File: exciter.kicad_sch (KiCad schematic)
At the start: 38 parts, among them U5 CC1200, X1 40MHz

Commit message: Add files via upload
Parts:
- removed R2 (x2): 10k, Resistor_SMD:R_0603_1608Metric, symbol Device:R_Small
- renumbered L1 to L2, L2 to L3, L3 to L4, L4 to L5, U5 to U6
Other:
- moved on the sheet: R2

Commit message: partial PN update
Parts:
- C5: PN (none) -> C0603C473K5RACTU
- C5: PN (none) -> C0603C103K5RAC7081
- C5: PN (none) -> C0603C102J5GAC7411
- C5: PN (none) -> C0603C104M5RAC7411
- C5: PN (none) -> GRM1885C1H152JA01D

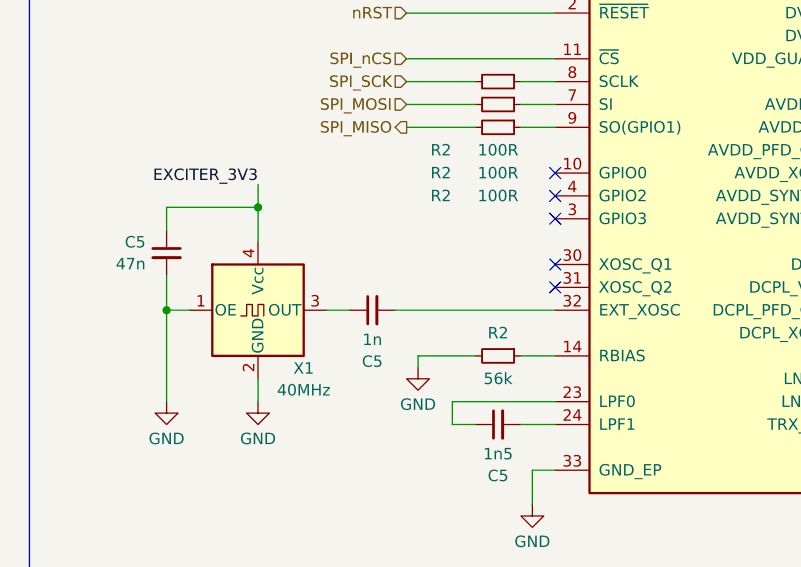
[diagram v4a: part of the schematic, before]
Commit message: added missing 40MHz source
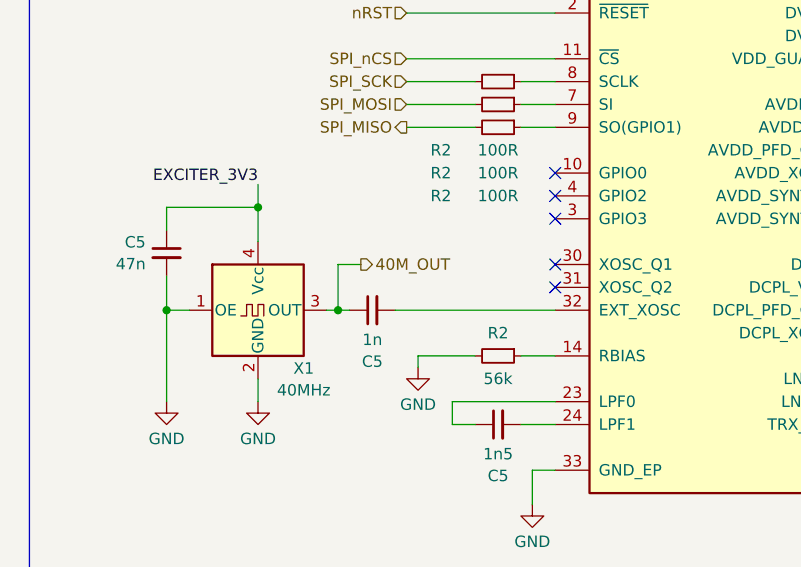
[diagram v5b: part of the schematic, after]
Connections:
- net 40M_OUT: now reaches C5.1, X1.3 (OUT)
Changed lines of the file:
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@@
   (junction (at 181.61 74.93) (diameter 0) (color 0 0 0 0)
+  )
+  (junction (at 116.84 107.95) (diameter 0) (color 0 0 0 0)
   )
   (junction (at 248.92 125.73) (diameter 0) (color 0 0 0 0)
@@
     (stroke (width 0) (type default))
   )
+  (wire (pts (xy 116.84 102.87) (xy 116.84 107.95))
+    (stroke (width 0) (type default))
+  )
   (wire (pts (xy 256.54 102.87) (xy 256.54 105.41))
     (stroke (width 0) (type default))
@@
     (stroke (width 0) (type default))
   )
+  (wire (pts (xy 119.38 102.87) (xy 116.84 102.87))
+    (stroke (width 0) (type default))
+  )
   (wire (pts (xy 247.65 111.76) (xy 247.65 110.49))
     (stroke (width 0) (type default))
@@
     (stroke (width 0) (type default))
   )
+  (wire (pts (xy 116.84 107.95) (xy 118.11 107.95))
+    (stroke (width 0) (type default))
+  )
   (wire (pts (xy 229.87 110.49) (xy 229.87 114.3))
     (stroke (width 0) (type default))
@@
     (stroke (width 0) (type default))
   )
-  (wire (pts (xy 115.57 107.95) (xy 118.11 107.95))
+  (wire (pts (xy 115.57 107.95) (xy 116.84 107.95))
     (stroke (width 0) (type default))
   )
@@
     (effects (font (size 1.27 1.27)) (justify right))
   )
+  (hierarchical_label "40M_OUT" (shape output) (at 119.38 102.87 0) (fields_autoplaced)
+    (effects (font (size 1.27 1.27)) (justify left))
+  )
   (symbol (lib_id "power:GND") (at 107.95 118.11 0) (unit 1)

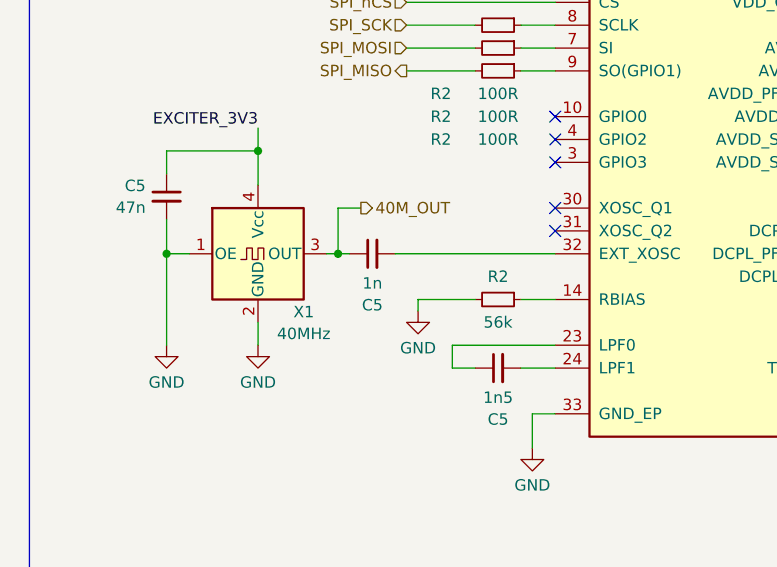
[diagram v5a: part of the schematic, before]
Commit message: caps' val update
40MHz TCXO's max. output load is 10p||10k
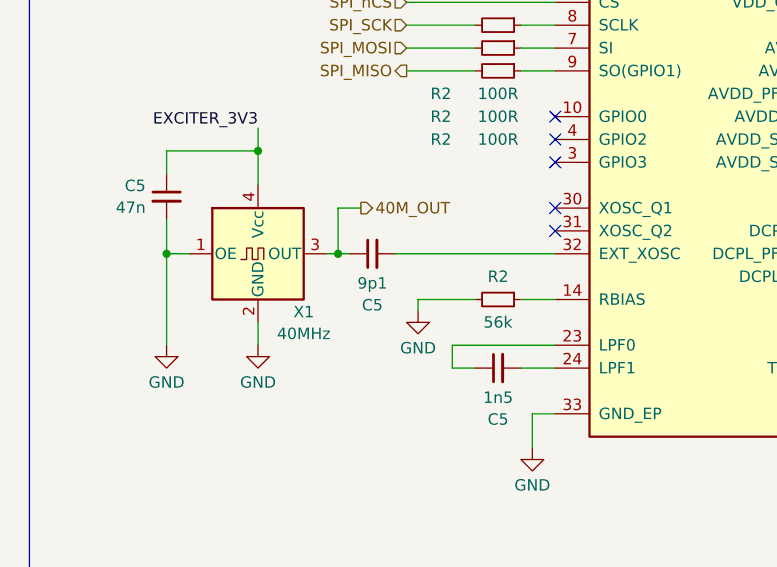
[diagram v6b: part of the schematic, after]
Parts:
- C5: value 1n -> 9p1; PN C0603C102J5GAC7411 -> (none)
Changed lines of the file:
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@@
       (effects (font (size 1.27 1.27)))
     )
-    (property "Value" "1n" (at 120.6563 111.2322 90)
+    (property "Value" "9p1" (at 120.6563 111.2322 90)
       (effects (font (size 1.27 1.27)))
     )
@@
       (effects (font (size 1.27 1.27)) hide)
     )
-    (property "PN" "C0603C102J5GAC7411" (at 120.65 107.95 0)
+    (property "PN" "" (at 120.65 107.95 0)
       (effects (font (size 1.27 1.27)) hide)
     )

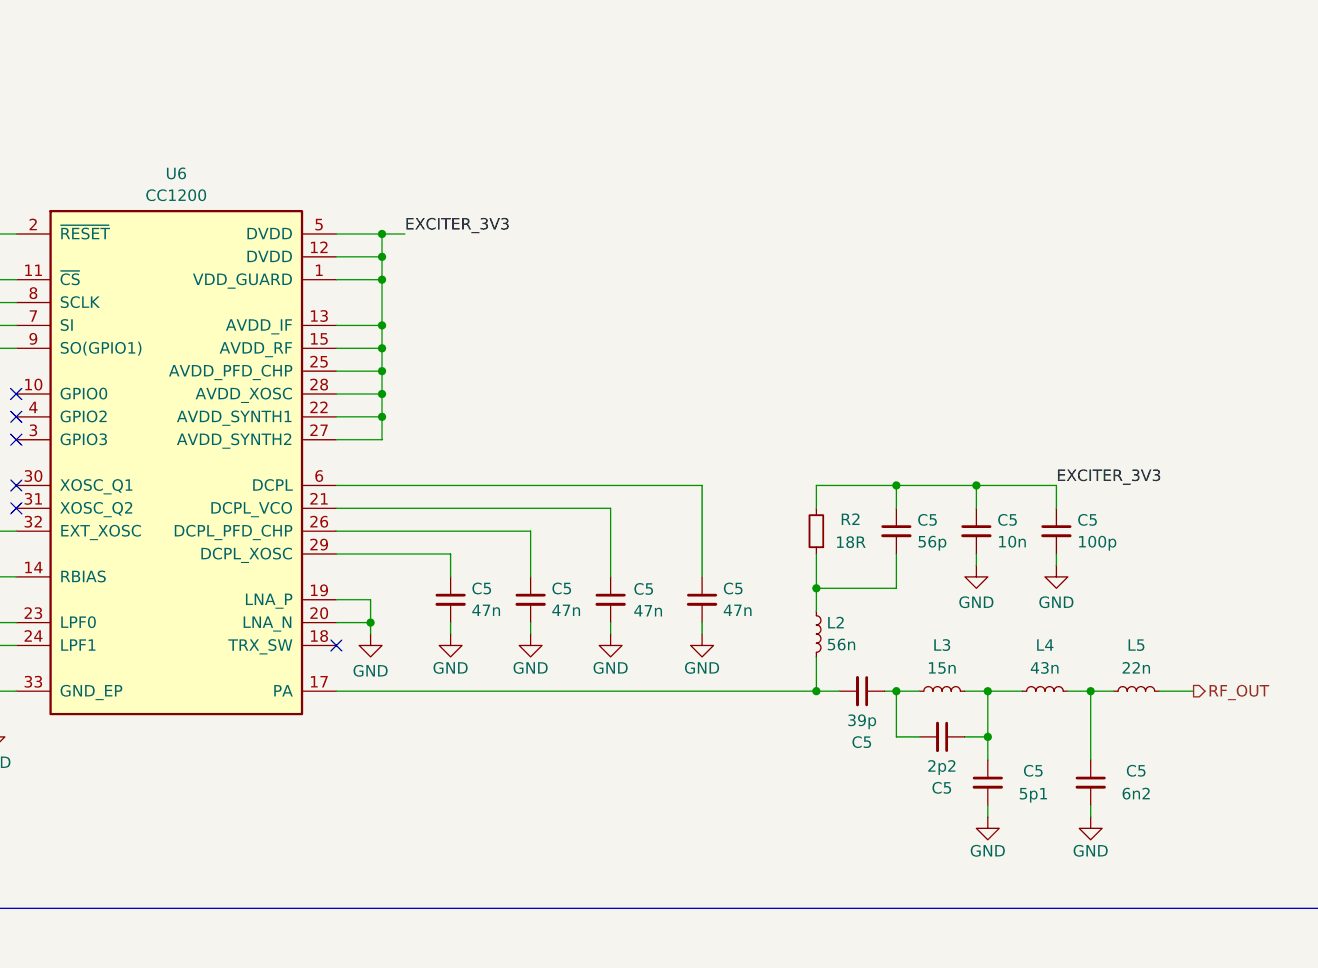
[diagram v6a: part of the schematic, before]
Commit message: significant updates
- supply for the detector block changed from 3.3V to 5V
- minor bugfixes
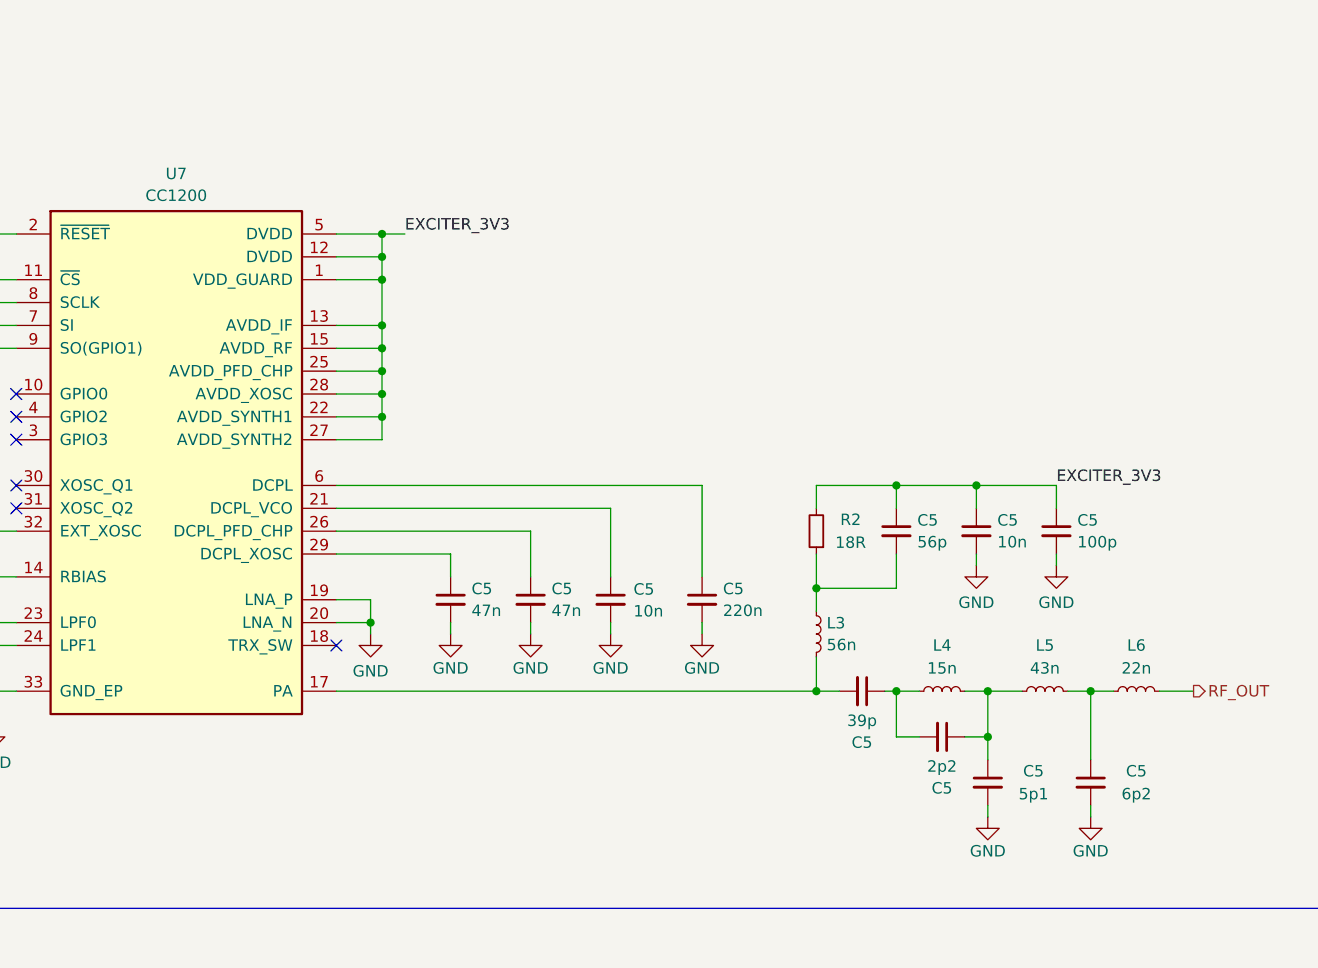
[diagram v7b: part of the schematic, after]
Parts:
- C5: value 47n -> 220n; PN C0603C473K5RACTU -> (none)
- C5: value 6n2 -> 6p2
- C5: value 47n -> 10n; PN C0603C473K5RACTU -> C0603C103K5RAC7081
- renumbered L2 to L3, L3 to L4, L4 to L5, L5 to L6, U6 to U7

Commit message: PN update
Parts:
- C5: PN (none) -> C0603C223K4RACTU
- C5: PN (none) -> 0603N560F500CT
- C5: PN (none) -> CL10C390JB81PNC
- C5: PN (none) -> GRM1885C1H6R2BA01D
- C5: PN (none) -> GRM1885C1H9R1BA01D
- C5: PN (none) -> CC0603BRNPO9BN2R2
- C5: PN (none) -> CC0603CRNPO9BN5R1
- C5: PN (none) -> VJ0603A101JXAPW1BC
- FB1: PN (none) -> BLM18KG601SH1D
- R2: PN (none) -> RC0603FR-0718RL
- U7: PN (none) -> CC1200RHBR
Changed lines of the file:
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@@
       (effects (font (size 1.27 1.27)) hide)
     )
-    (property "PN" "" (at 217.17 115.57 0)
+    (property "PN" "C0603C223K4RACTU" (at 217.17 115.57 0)
       (effects (font (size 1.27 1.27)) hide)
     )
@@
       (effects (font (size 1.27 1.27)) hide)
     )
-    (property "PN" "" (at 186.69 198.12 90)
+    (property "PN" "BLM18KG601SH1D" (at 186.69 198.12 90)
       (effects (font (size 1.27 1.27)) hide)
     )
@@
       (effects (font (size 1.27 1.27)) hide)
     )
+    (property "PN" "0603N560F500CT" (at 238.76 107.95 0)
+      (effects (font (size 1.27 1.27)) hide)
+    )
     (pin "1")
     (pin "2")
@@
       (effects (font (size 1.27 1.27)) hide)
     )
+    (property "PN" "CL10C390JB81PNC" (at 234.95 125.73 0)
+      (effects (font (size 1.27 1.27)) hide)
+    )
     (pin "1")
     (pin "2")
@@
       (effects (font (size 1.27 1.27)) hide)
     )
+    (property "PN" "GRM1885C1H6R2BA01D" (at 260.35 135.89 0)
+      (effects (font (size 1.27 1.27)) hide)
+    )
     (pin "1")
     (pin "2")
@@
       (effects (font (size 1.27 1.27)) hide)
     )
-    (property "PN" "" (at 120.65 107.95 0)
+    (property "PN" "GRM1885C1H9R1BA01D" (at 120.65 107.95 0)
       (effects (font (size 1.27 1.27)) hide)
     )
@@
     )
     (property "Datasheet" "http://www.ti.com/lit/ds/symlink/cc1200.pdf" (at 146.05 71.12 0)
+      (effects (font (size 1.27 1.27)) hide)
+    )
+    (property "PN" "CC1200RHBR" (at 158.75 100.33 0)
       (effects (font (size 1.27 1.27)) hide)
     )
@@
       (effects (font (size 1.27 1.27)) hide)
     )
+    (property "PN" "CC0603BRNPO9BN2R2" (at 243.84 130.81 0)
+      (effects (font (size 1.27 1.27)) hide)
+    )
     (pin "1")
     (pin "2")
@@
       (effects (font (size 1.27 1.27)) hide)
     )
-    (property "PN" "" (at 229.87 107.95 0)
+    (property "PN" " RC0603FR-0718RL " (at 229.87 107.95 0)
       (effects (font (size 1.27 1.27)) hide)
     )
@@
       (effects (font (size 1.27 1.27)) hide)
     )
+    (property "PN" "CC0603CRNPO9BN5R1" (at 248.92 135.89 0)
+      (effects (font (size 1.27 1.27)) hide)
+    )
     (pin "1")
     (pin "2")
@@
       (effects (font (size 1.27 1.27)) hide)
     )
+    (property "PN" "VJ0603A101JXAPW1BC" (at 256.54 107.95 0)
+      (effects (font (size 1.27 1.27)) hide)
+    )
